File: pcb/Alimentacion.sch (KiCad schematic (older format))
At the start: 5 parts, among them U6 TSR_1

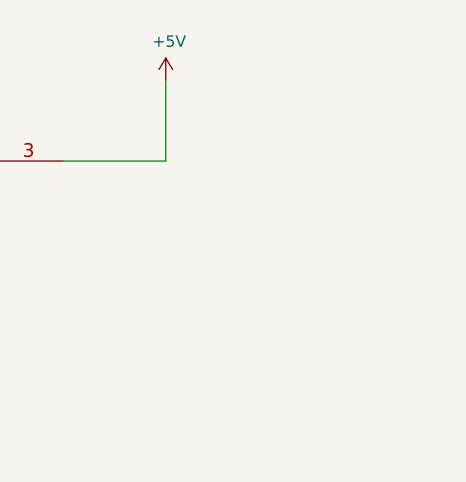
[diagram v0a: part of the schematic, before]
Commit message: finalizado el posicionado sobre la pcb
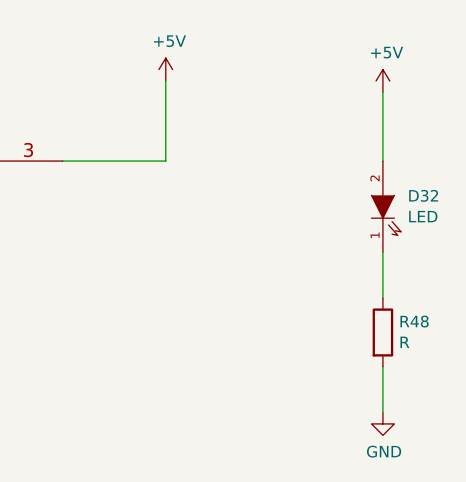
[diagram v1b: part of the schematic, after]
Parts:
- added D32: LED, Leds:LED_0805, symbol LED
- added R48: R, Resistors_SMD:R_0805, symbol R
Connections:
- net +5V: now also D32.2 (A)
- net GND: now also R48.2
- new net: D32.1 (K), R48.1
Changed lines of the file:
@@
 $EndDescr
 $Comp
-L GND #PWR061
+L GND #PWR063
 U 1 1 5768B46A
 P 1550 2150
-F 0 "#PWR061" H 1550 1900 50  0001 C CNN
+F 0 "#PWR063" H 1550 1900 50  0001 C CNN
 F 1 "GND" H 1555 1977 50  0000 C CNN
 F 2 "" H 1550 2150 50  0000 C CNN
@@
 $EndComp
 $Comp
-L PWR_FLAG #FLG062
+L PWR_FLAG #FLG064
 U 1 1 5768B47E
 P 1550 1950
-F 0 "#FLG062" H 1550 2045 50  0001 C CNN
+F 0 "#FLG064" H 1550 2045 50  0001 C CNN
 F 1 "PWR_FLAG" H 1550 2174 50  0000 C CNN
 F 2 "" H 1550 1950 50  0000 C CNN
@@
 	1550 1950 1550 2150
 $Comp
-L VSS #PWR063
+L VSS #PWR065
 U 1 1 576A7AE8
 P 2000 1900
-F 0 "#PWR063" H 2000 1750 50  0001 C CNN
+F 0 "#PWR065" H 2000 1750 50  0001 C CNN
 F 1 "VSS" H 2017 2073 50  0000 C CNN
 F 2 "" H 2000 1900 50  0000 C CNN
@@
 $EndComp
 $Comp
-L PWR_FLAG #FLG064
+L PWR_FLAG #FLG066
 U 1 1 576A7AFA
 P 2000 2100
-F 0 "#FLG064" H 2000 2195 50  0001 C CNN
+F 0 "#FLG066" H 2000 2195 50  0001 C CNN
 F 1 "PWR_FLAG" H 2000 2323 50  0000 C CNN
 F 2 "" H 2000 2100 50  0000 C CNN
@@
 	2950 3000 2950 2900
 $Comp
-L +5V #PWR065
+L +5V #PWR067
 U 1 1 576A82A8
 P 2950 2900
-F 0 "#PWR065" H 2950 2750 50  0001 C CNN
+F 0 "#PWR067" H 2950 2750 50  0001 C CNN
 F 1 "+5V" H 2965 3073 50  0000 C CNN
 F 2 "" H 2950 2900 50  0000 C CNN
@@
 	7350 2500 7350 2700
 $Comp
-L GND #PWR066
+L GND #PWR068
 U 1 1 576F176B
 P 7350 2700
-F 0 "#PWR066" H 7350 2450 50  0001 C CNN
+F 0 "#PWR068" H 7350 2450 50  0001 C CNN
 F 1 "GND" H 7355 2527 50  0000 C CNN
 F 2 "" H 7350 2700 50  0000 C CNN
@@
 $EndComp
 $Comp
-L GND #PWR067
+L GND #PWR069
 U 1 1 576F178C
 P 6150 2700
-F 0 "#PWR067" H 6150 2450 50  0001 C CNN
+F 0 "#PWR069" H 6150 2450 50  0001 C CNN
 F 1 "GND" H 6155 2527 50  0000 C CNN
 F 2 "" H 6150 2700 50  0000 C CNN
@@
 $EndComp
 $Comp
-L GND #PWR068
+L GND #PWR070
 U 1 1 576F17A6
 P 4950 2700
-F 0 "#PWR068" H 4950 2450 50  0001 C CNN
+F 0 "#PWR070" H 4950 2450 50  0001 C CNN
 F 1 "GND" H 4955 2527 50  0000 C CNN
 F 2 "" H 4950 2700 50  0000 C CNN
@@
 	8550 1950 8550 1600
 $Comp
-L +5V #PWR069
+L +5V #PWR071
 U 1 1 576F18D7
 P 8550 1600
-F 0 "#PWR069" H 8550 1450 50  0001 C CNN
+F 0 "#PWR071" H 8550 1450 50  0001 C CNN
 F 1 "+5V" H 8565 1773 50  0000 C CNN
 F 2 "" H 8550 1600 50  0000 C CNN
@@
 	4500 1950 4500 1850
 $Comp
-L PWR_FLAG #FLG070
+L PWR_FLAG #FLG072
 U 1 1 576F3DE8
 P 6500 1600
-F 0 "#FLG070" H 6500 1695 50  0001 C CNN
+F 0 "#FLG072" H 6500 1695 50  0001 C CNN
 F 1 "PWR_FLAG" H 6500 1824 50  0000 C CNN
 F 2 "" H 6500 1600 50  0000 C CNN
@@
 Connection ~ 6500 1950
 $Comp
-L +24V #PWR071
+L +24V #PWR073
 U 1 1 576F9726
 P 2400 1900
-F 0 "#PWR071" H 2400 1750 50  0001 C CNN
+F 0 "#PWR073" H 2400 1750 50  0001 C CNN
 F 1 "+24V" H 2415 2073 50  0000 C CNN
 F 2 "" H 2400 1900 50  0000 C CNN
@@
 $EndComp
 $Comp
-L PWR_FLAG #FLG072
+L PWR_FLAG #FLG074
 U 1 1 576F9747
 P 2400 2100
-F 0 "#FLG072" H 2400 2195 50  0001 C CNN
+F 0 "#FLG074" H 2400 2195 50  0001 C CNN
 F 1 "PWR_FLAG" H 2400 2323 50  0000 C CNN
 F 2 "" H 2400 2100 50  0000 C CNN
@@
 	2400 2100 2400 1900
 $Comp
-L +24V #PWR073
+L +24V #PWR075
 U 1 1 5786CF27
 P 4500 1850
-F 0 "#PWR073" H 4500 1700 50  0001 C CNN
+F 0 "#PWR075" H 4500 1700 50  0001 C CNN
 F 1 "+24V" H 4515 2023 50  0000 C CNN
 F 2 "" H 4500 1850 50  0000 C CNN
@@
 	1    0    0    -1
 $EndComp
+$Comp
+L LED D32
+U 1 1 578EC7B5
+P 9500 2150
+F 0 "D32" V 9546 2042 50  0000 R CNN
+F 1 "LED" V 9455 2042 50  0000 R CNN
+F 2 "Leds:LED_0805" H 9500 2150 50  0001 C CNN
+F 3 "" H 9500 2150 50  0000 C CNN
+	1    9500 2150
+	0    -1   -1   0
+$EndComp
+$Comp
+L R R48
+U 1 1 578EC80E
+P 9500 2700
+F 0 "R48" H 9570 2746 50  0000 L CNN
+F 1 "R" H 9570 2655 50  0000 L CNN
+F 2 "Resistors_SMD:R_0805" V 9430 2700 50  0001 C CNN
+F 3 "" H 9500 2700 50  0000 C CNN
+	1    9500 2700
+	1    0    0    -1
+$EndComp
+$Comp
+L GND #PWR076
+U 1 1 578EC855
+P 9500 3050
+F 0 "#PWR076" H 9500 2800 50  0001 C CNN
+F 1 "GND" H 9505 2877 50  0000 C CNN
+F 2 "" H 9500 3050 50  0000 C CNN
+F 3 "" H 9500 3050 50  0000 C CNN
+	1    9500 3050
+	1    0    0    -1
+$EndComp
+Wire Wire Line
+	9500 3050 9500 2850
+Wire Wire Line
+	9500 2550 9500 2350
+Wire Wire Line
+	9500 1950 9500 1650
+$Comp
+L +5V #PWR077
+U 1 1 578EC8CB
+P 9500 1650
+F 0 "#PWR077" H 9500 1500 50  0001 C CNN
+F 1 "+5V" H 9515 1823 50  0000 C CNN
+F 2 "" H 9500 1650 50  0000 C CNN
+F 3 "" H 9500 1650 50  0000 C CNN
+	1    9500 1650
+	1    0    0    -1
+$EndComp
